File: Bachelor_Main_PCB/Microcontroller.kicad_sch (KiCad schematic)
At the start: 40 parts, among them J3 M20-9990245, J4 M20-9990245, J5 M20-9990245, U3 STM32H7A3ZITxQ, U4 USB3320C-EZK-TR, Y1 SG-210STF 24Mhz

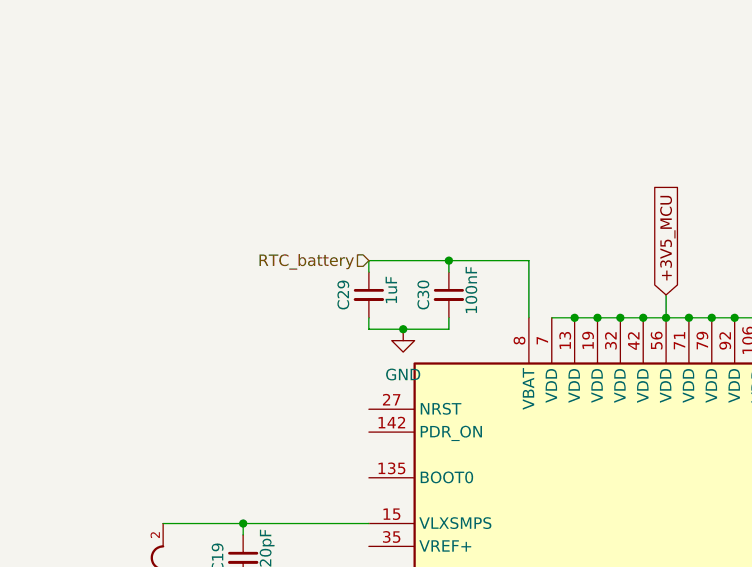
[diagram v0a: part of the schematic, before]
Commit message: add BK-916 rtc battery holder
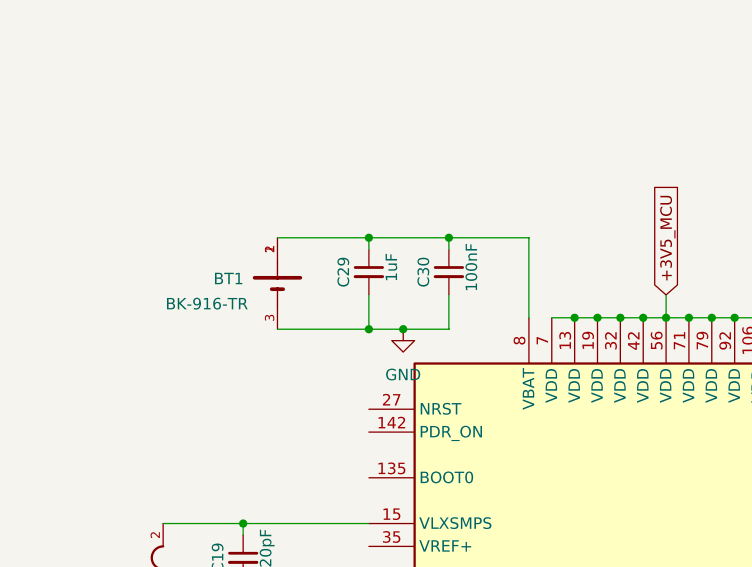
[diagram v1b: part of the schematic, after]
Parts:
- added BT1: BK-916-TR, BK-916-TR:BAT_BK-916-TR, symbol BK-916-TR:BK-916-TR
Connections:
- net GND: now also BT1.3
- net RTC_battery: no longer names the net of C29.1, C30.1, U3.8 (VBAT)
- net RTC_battery: now also BT1.1, BT1.2
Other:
- moved on the sheet: C29, C30

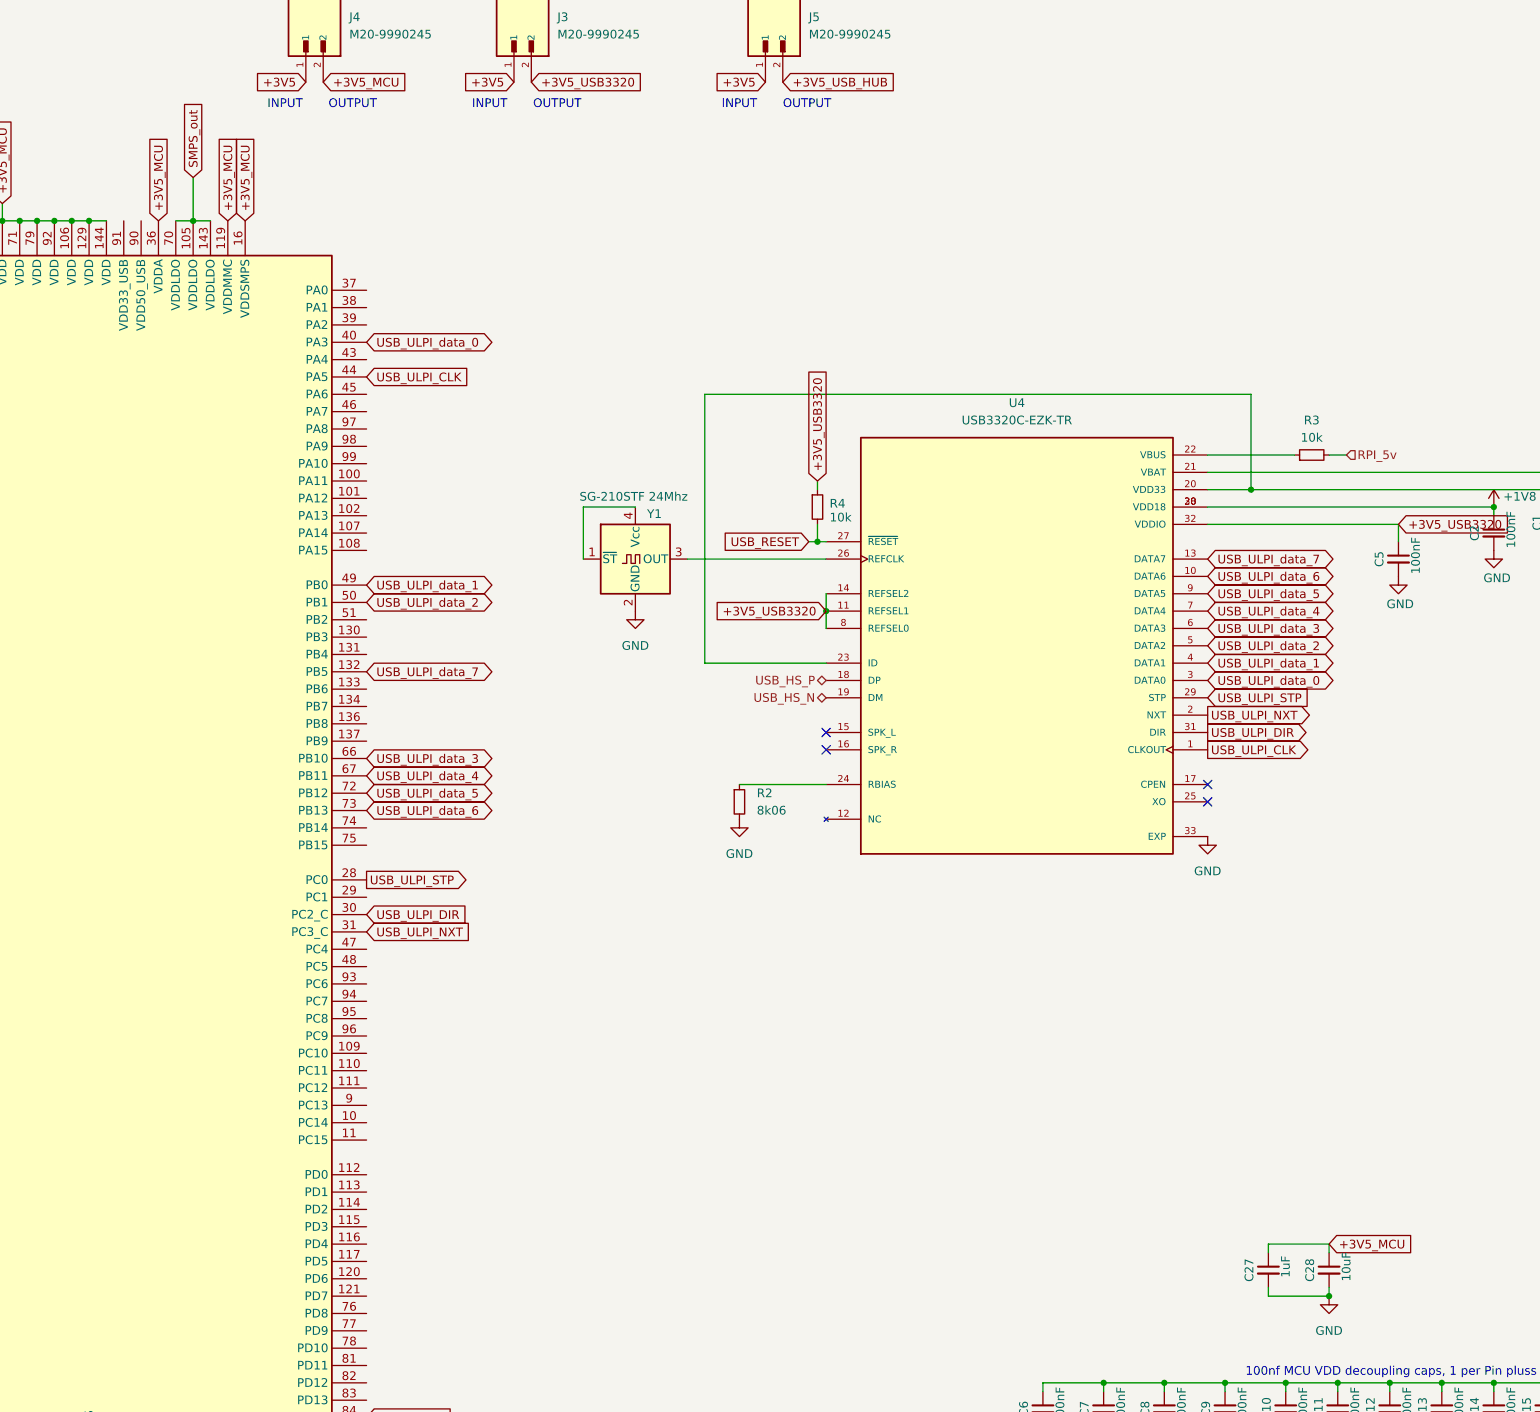
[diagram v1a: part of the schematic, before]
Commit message: VDDUSB headers together
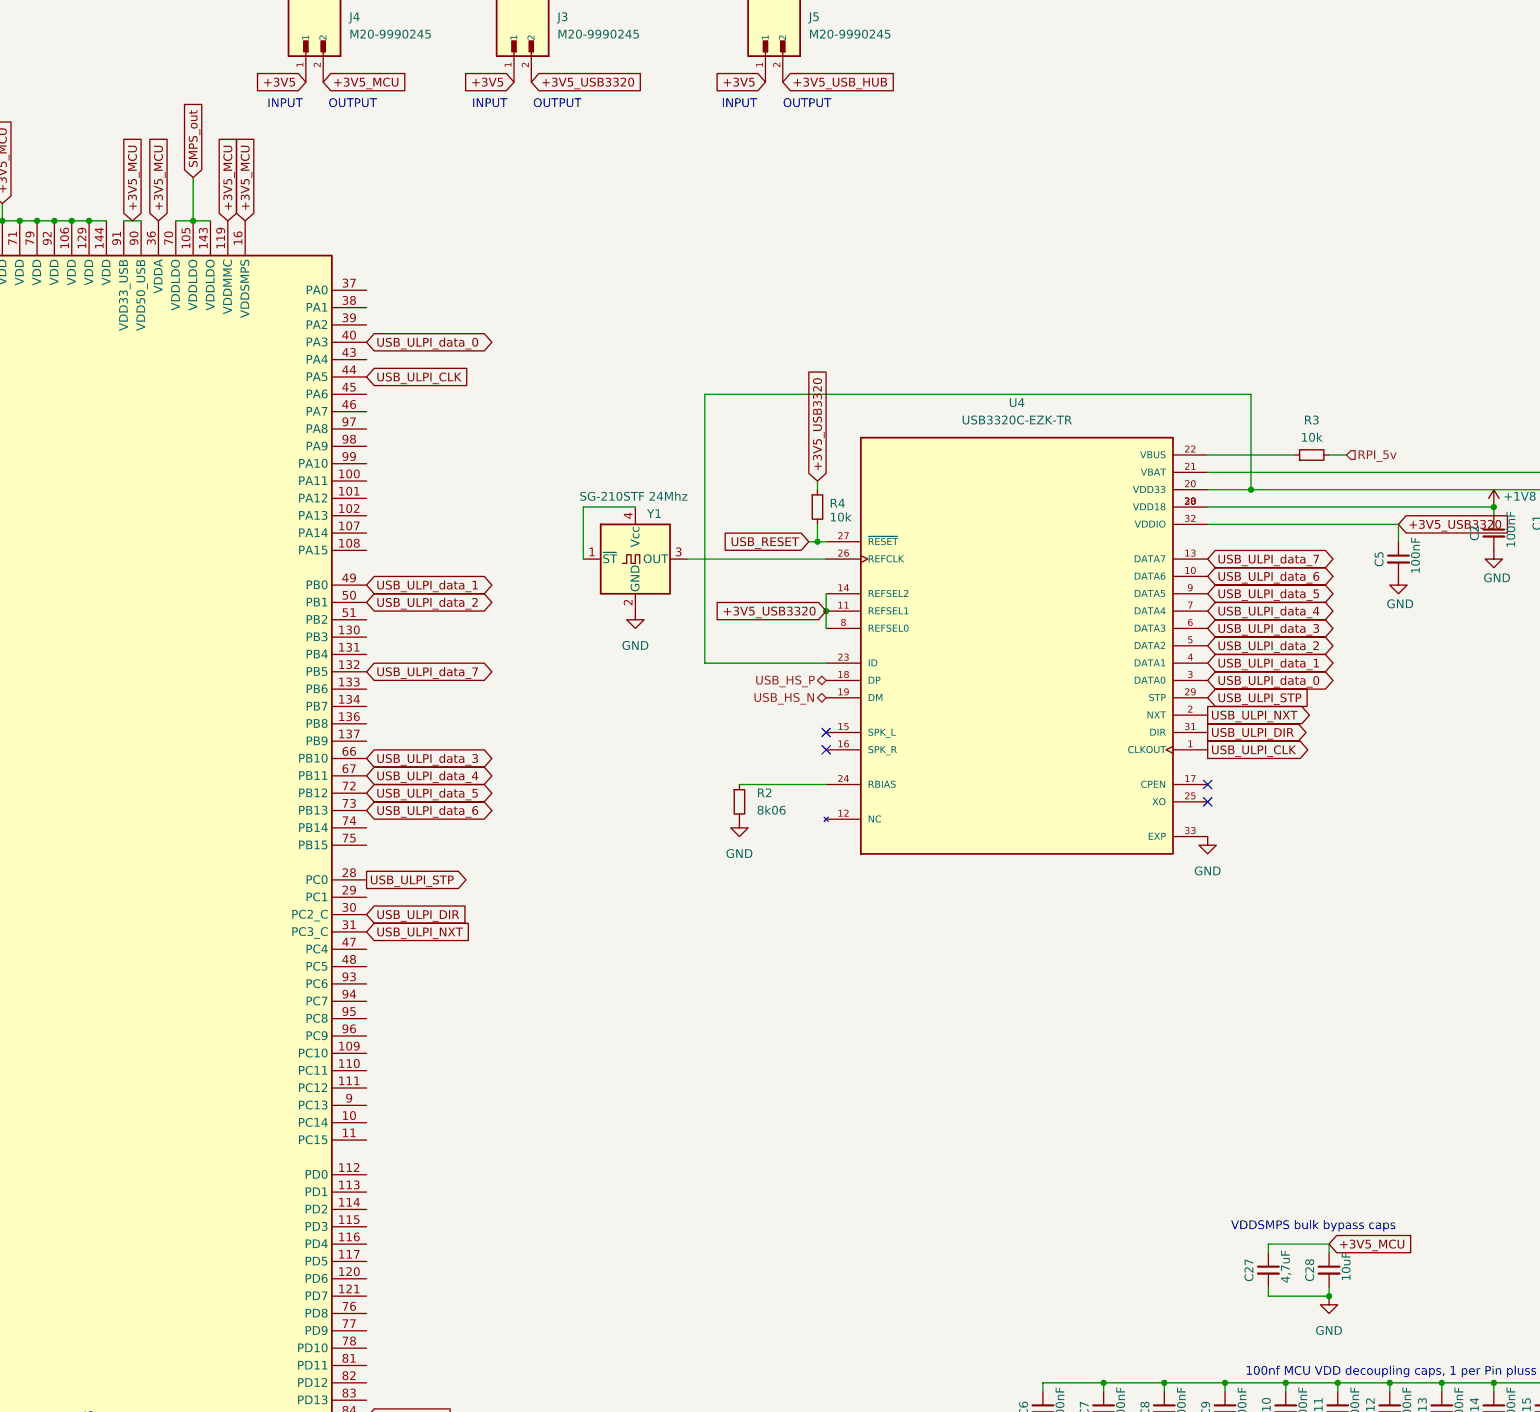
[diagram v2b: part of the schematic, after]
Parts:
- C27: value 1uF -> 4,7uF
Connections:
- net +3V5_MCU: now also U3.90 (VDD50_USB), U3.91 (VDD33_USB)
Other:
- note added: "VDDSMPS bulk bypass caps"

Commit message: PDR_on to VDD
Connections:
- net +3V5_MCU: now also U3.142 (PDR_ON), U3.35 (VREF+)
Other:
- moved on the sheet: C19

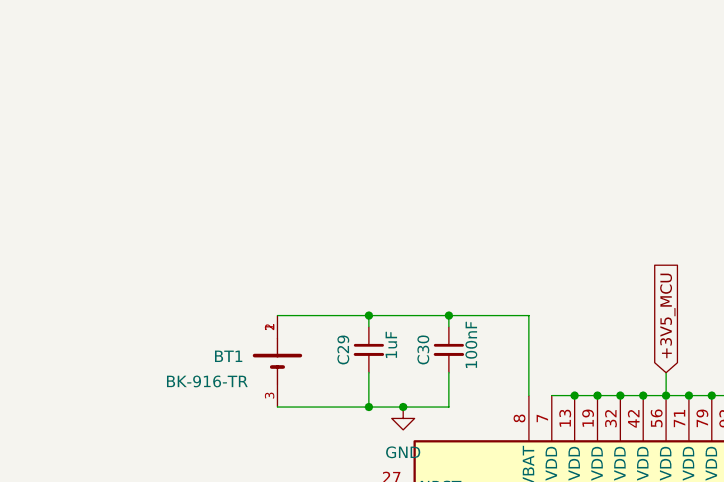
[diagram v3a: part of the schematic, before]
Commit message: Add RTC oscillator
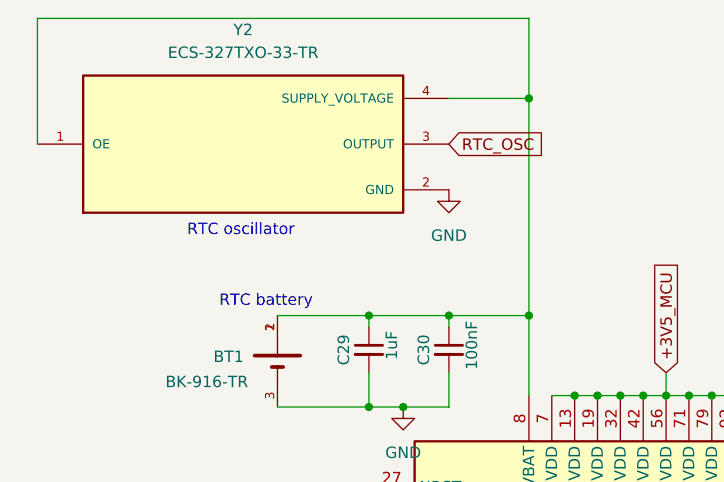
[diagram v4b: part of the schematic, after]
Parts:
- added Y2: ECS-327TXO-33-TR, ECS-327TXO-33-TR:OSC_ECS-327TXO-33-TR, symbol ECS-327TXO-33-TR:ECS-327TXO-33-TR
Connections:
- net GND: now also Y2.2 (GND)
- net at BT1.1, BT1.2, C29.1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: now also Y2.1 (OE), Y2.4 (SUPPLY_VOLTAGE)
- new net RTC_OSC: Y2.3 (OUTPUT)
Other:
- note added: "RTC battery"
- note added: "RTC oscillator"

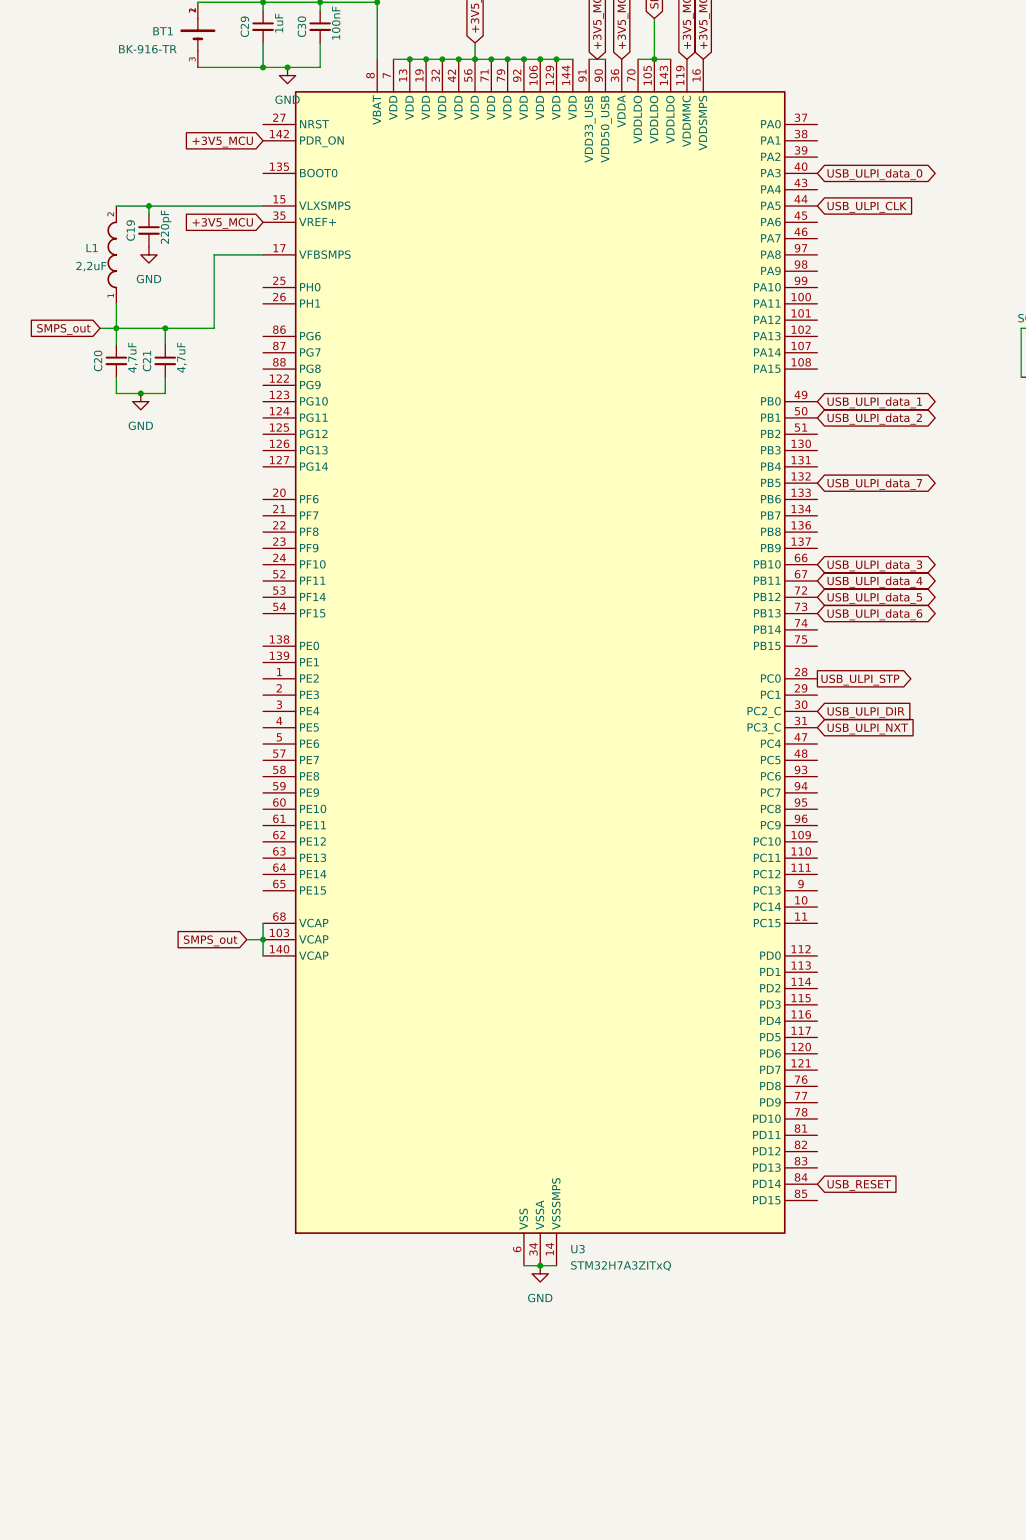
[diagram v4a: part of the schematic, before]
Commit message: ADD JTAG 7pin header
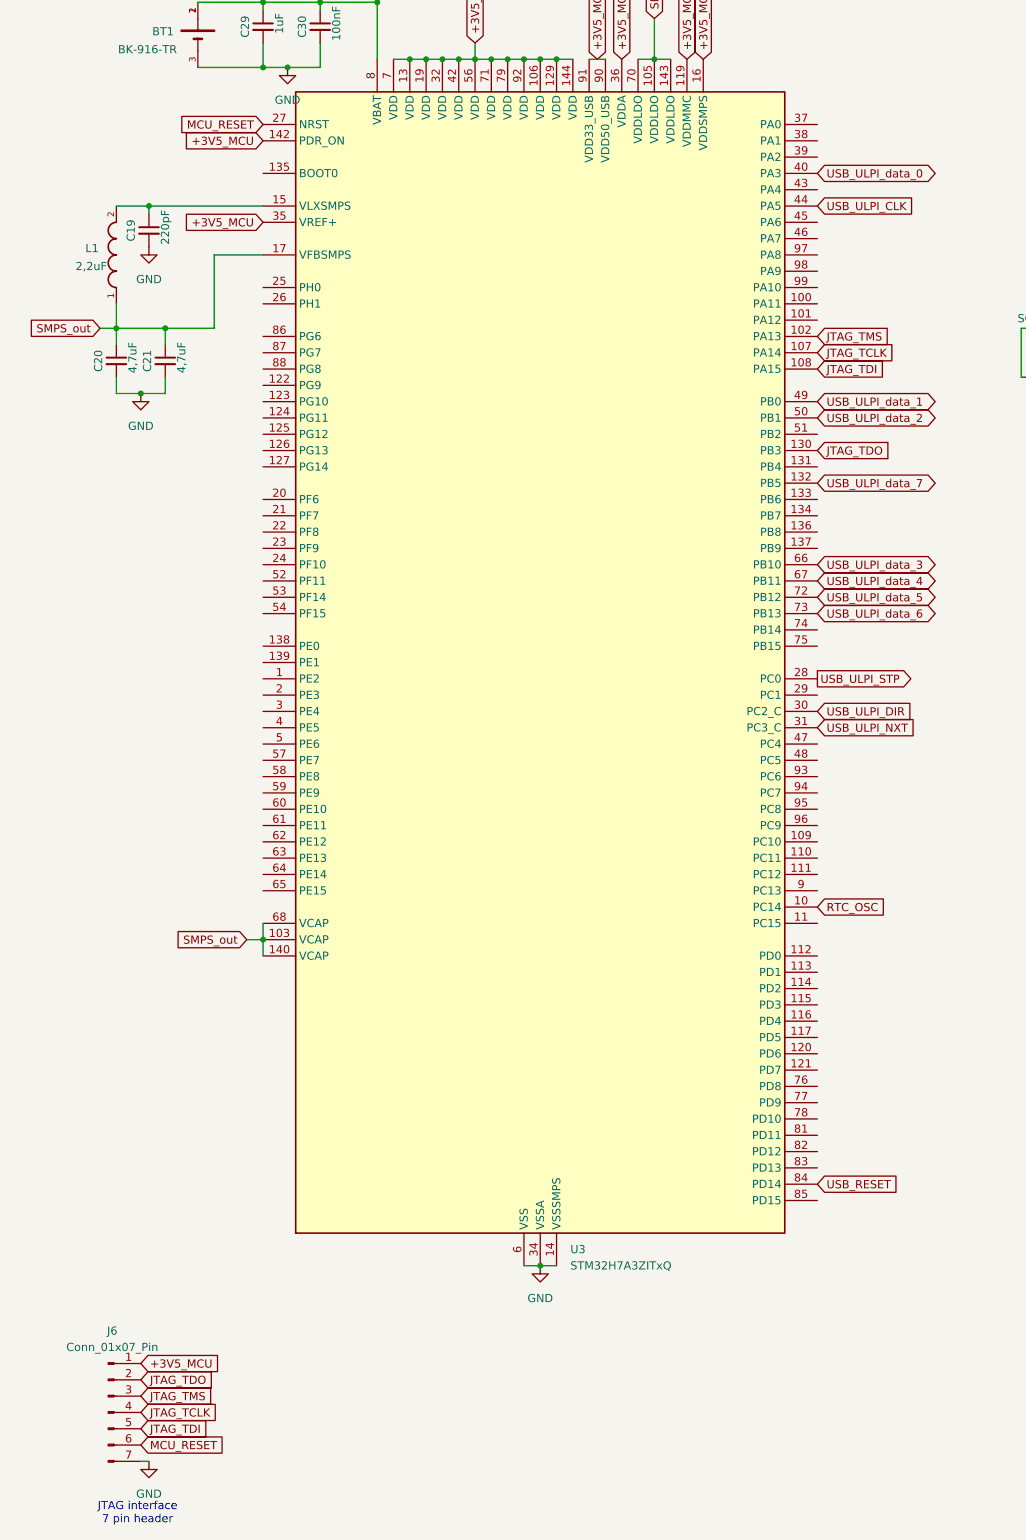
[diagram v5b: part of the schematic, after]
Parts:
- added J6: Conn_01x07_Pin, Connector_PinHeader_2.54mm:PinHeader_1x07_P2.54mm_Vertical, symbol Connector:Conn_01x07_Pin
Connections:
- net +3V5_MCU: now also J6.1 (Pin_1)
- net GND: now also J6.7 (Pin_7)
- net RTC_OSC: now also U3.10 (PC14)
- net JTAG_TMS: now reaches U3.102 (PA13)
- net JTAG_TMS: now also J6.3 (Pin_3)
- net JTAG_TCLK: now reaches U3.107 (PA14)
- net JTAG_TCLK: now also J6.4 (Pin_4)
- net JTAG_TDI: now reaches U3.108 (PA15)
- net JTAG_TDI: now also J6.5 (Pin_5)
- net JTAG_TDO: now reaches U3.130 (PB3)
- net JTAG_TDO: now also J6.2 (Pin_2)
- net MCU_RESET: now reaches U3.27 (NRST)
- net MCU_RESET: now also J6.6 (Pin_6)
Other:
- note added: "JTAG interface 7 pin header"
